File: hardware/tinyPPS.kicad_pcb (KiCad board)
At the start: 2 copper layers, 63 x 37 mm, 63 parts, among them IC1 AP2205-33Y-13, IC2 AP33772SDKZ-13-FA01, J1 USB_C_Receptacle_USB2.0_14P, J2 187-3802, J3 187-3802, J5 SM03B-SRSS-TB_LF__SN_, Q1 DMN3009SFG-7, Q2 DMN3009SFG-7, Q3 BSS123, Q4 BSS123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

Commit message: Minor changes on the PCB
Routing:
- net Net-(Q1-G): track 14.6 -> 13.6 mm
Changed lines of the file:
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@@
 	)
 	(gr_text "DBG"
-		(at 104.35 109.05 0)
+		(at 101.3 108.8 0)
 		(layer "F.SilkS")
 		(effects
@@
 	)
 	(segment
-		(start 118.72 89.32)
-		(end 118.7 89.3)
-		(width 0.3)
-		(layer "F.Cu")
-		(net 80)
-	)
-	(segment
-		(start 118.72 90)
-		(end 118.72 89.32)
+		(start 124.8405 85.7095)
+		(end 124.85 85.7)
 		(width 0.3)
 		(layer "F.Cu")
@@
 	)
 	(segment
-		(start 124.8405 85.7095)
-		(end 124.85 85.7)
+		(start 119.4 90)
+		(end 118.72 90)
 		(width 0.3)
 		(layer "F.Cu")
@@
 	)
 	(via
-		(at 118.7 89.3)
+		(at 119.4 90)
 		(size 0.6)
 		(drill 0.3)
@@
 	)
 	(segment
-		(start 124.85 85.7)
-		(end 124.85 89.3)
+		(start 119.4 90)
+		(end 120.4 91)
 		(width 0.3)
 		(layer "B.Cu")
@@
 	)
 	(segment
-		(start 124.85 89.3)
-		(end 124.85 91)
+		(start 124.85 85.7)
+		(end 124.85 89.3)
 		(width 0.3)
 		(layer "B.Cu")
@@
 	)
 	(segment
-		(start 124.85 91)
-		(end 120.4 91)
+		(start 120.4 91)
+		(end 124.85 91)
 		(width 0.3)
 		(layer "B.Cu")
@@
 	)
 	(segment
-		(start 120.4 91)
-		(end 118.7 89.3)
+		(start 124.85 89.3)
+		(end 124.85 91)
 		(width 0.3)
 		(layer "B.Cu")

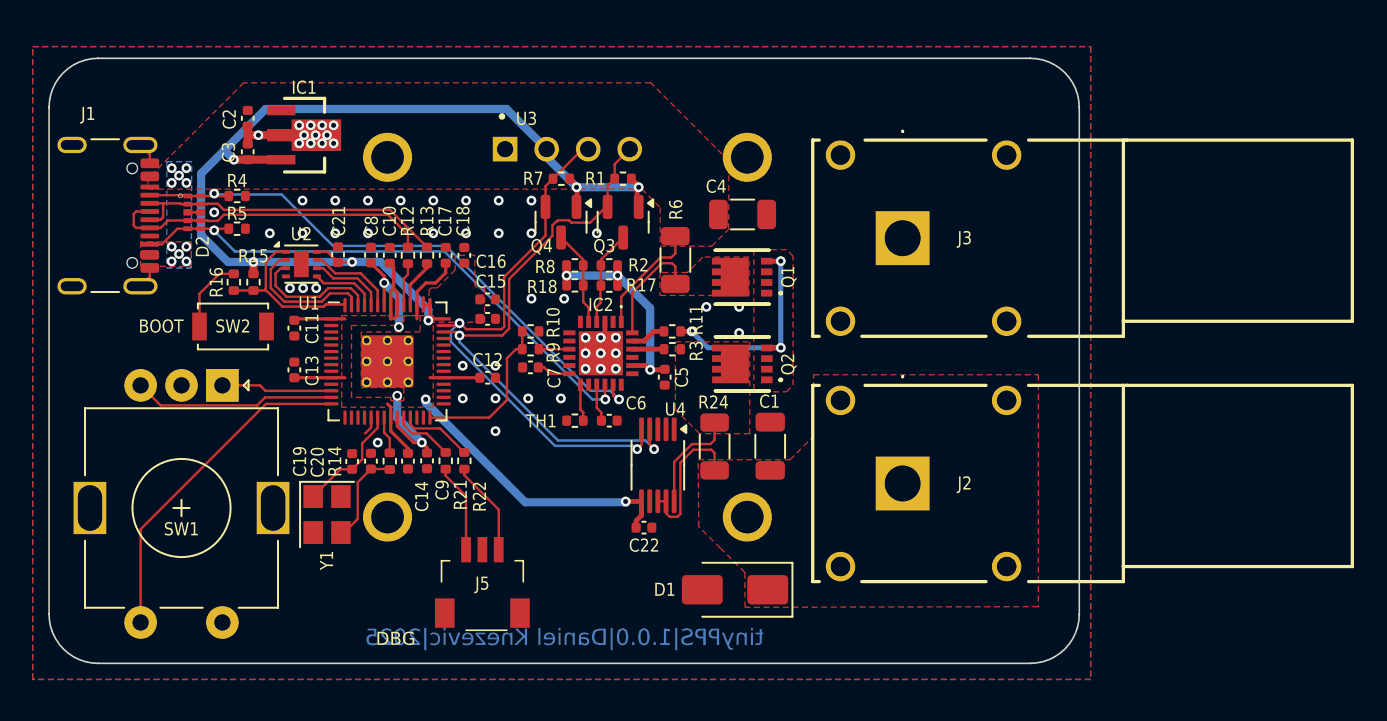
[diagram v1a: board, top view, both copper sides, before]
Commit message: Change rotary encoder to a horizontal type
- Re-route the PCB
- Make PCB with smaller (60mm)
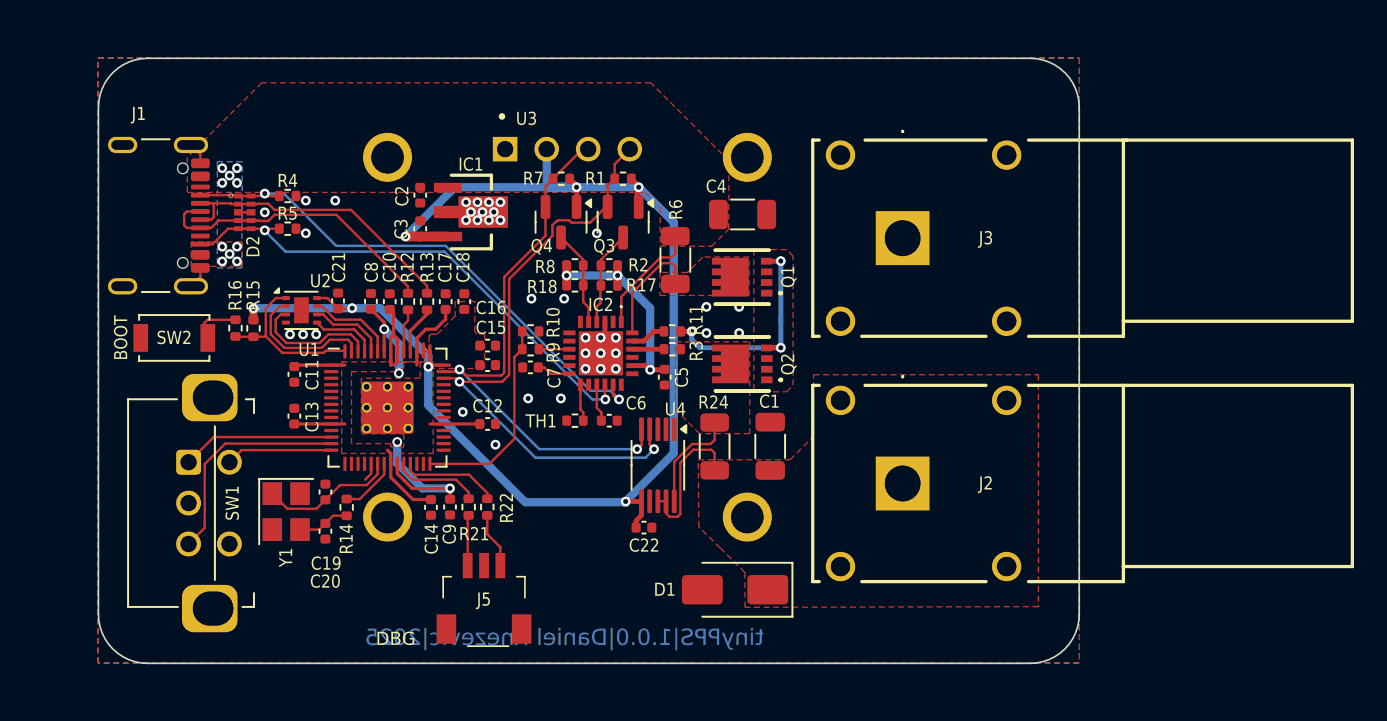
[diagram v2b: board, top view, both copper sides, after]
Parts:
- R3: value 27R -> 100R
- SW1: footprint Rotary_Encoder:RotaryEncoder_Alps_EC11E-Switch_Vertical_H20mm -> Rotary_Encoder:EC11 horizontal
- moved C2 11.5 mm to (102.8, 81.7)
- moved C3 11.5 mm to (102.8, 83.7)
- moved IC1 11.2 mm to (105.9, 82.7)
- moved SW1 6.22 mm to (86.6, 98.0), turned to 0 degrees
- moved C20 5.11 mm to (97.0, 102.2), turned to -90 degrees
- moved R14 3.87 mm to (98.3, 100.8)
- moved SW2 3.66 mm to (87.8, 90.4), turned to 0 degrees
- moved C14 3.16 mm to (103.5, 100.8)
- moved C9 3.16 mm to (104.6, 100.7)
- moved R21 3.16 mm to (105.8, 100.7)
- moved R22 3.16 mm to (106.9, 100.7)
- moved D2 3.09 mm to (92.1, 82.7)
- moved R4 3.09 mm to (94.7, 81.7)
- moved R5 3.09 mm to (94.7, 83.7)
- moved J1 3.09 mm to (85.7, 82.9)
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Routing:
- net /GPIO11: track 20.5 -> 6.53 mm
- net +3V3: track 101.1 -> 105.7 mm, vias 8 -> 7
- net +1V1: track 17.3 -> 20.5 mm
- net /CC2: track 35.2 -> 32.1 mm
- net /CC1: track 35.9 -> 32.8 mm
- net GND: track 9.71 -> 6.79 mm, vias 55 -> 38
- net /PD_INT: track 9.76 -> 12.4 mm
- net /GPIO9: track 6.80 -> 9.36 mm
- net Net-(C20-Pad1): track 5.73 -> 3.20 mm
- net Net-(J5-Pad3): track 5.80 -> 3.40 mm
- net Net-(J5-Pad1): track 5.44 -> 3.10 mm
- net /USB_D+: track 20.0 -> 17.9 mm
- net /SDA: track 36.0 -> 37.8 mm
- net /~{USB_BOOT}: track 4.61 -> 2.89 mm
- net /USB_D-: track 20.0 -> 18.4 mm
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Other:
- board size 63 x 37 mm -> 60 x 37 mm

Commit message: Update PCB routing - use +3v3 and GND planes
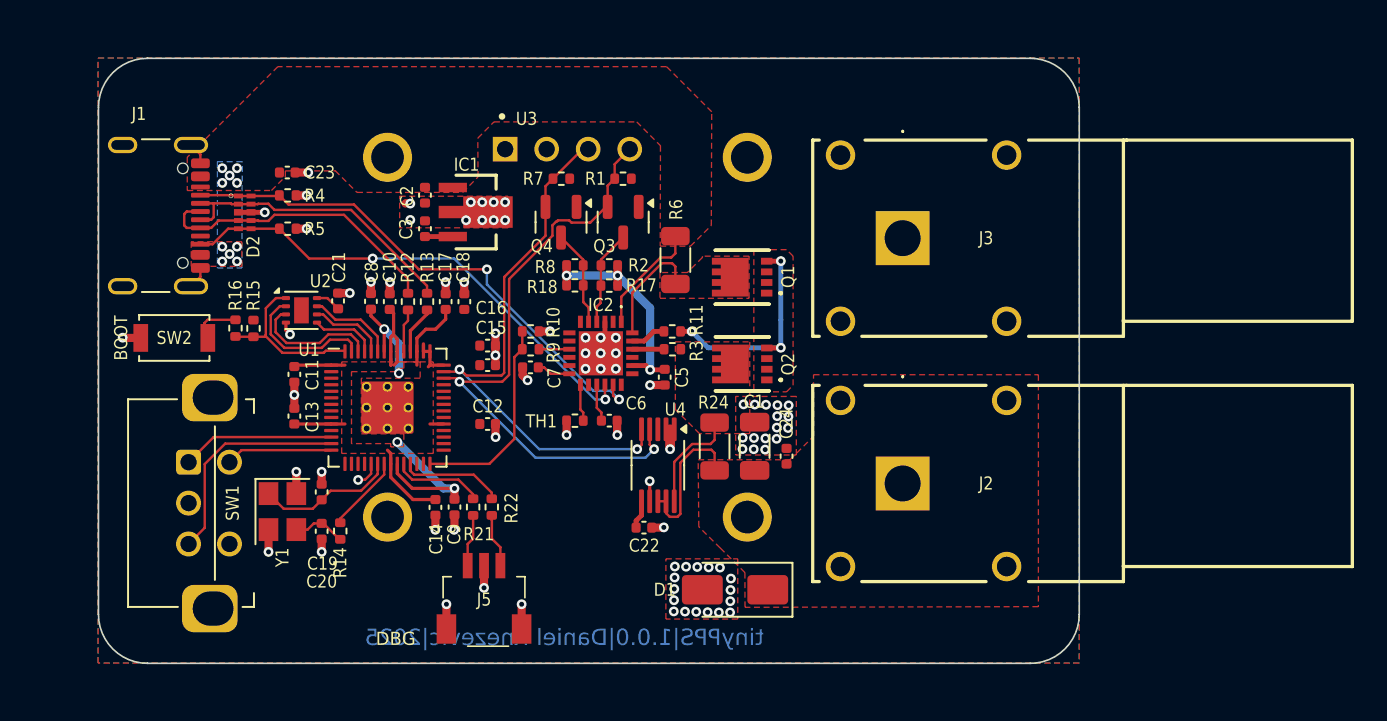
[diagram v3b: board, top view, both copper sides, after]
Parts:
- removed C4: 10u, Capacitor_SMD:C_1206_3216Metric
- added C23: 100n, Capacitor_SMD:C_0402_1005Metric, F.Cu at (94.7, 80.3)
- added C24: 100n, Capacitor_SMD:C_0402_1005Metric, F.Cu at (125.2, 97.6)
- moved R14 1.50 mm to (97.9, 102.2)
- moved C1 0.95 mm to (123.2, 97.0)
- moved C2 0.29 mm to (103.1, 81.7)
- moved C3 0.29 mm to (103.1, 83.7)
- moved IC1 0.29 mm to (106.2, 82.7)
- moved C14 0.27 mm to (103.7, 100.8)
- moved C9 0.27 mm to (104.9, 100.7)
- moved R21 0.27 mm to (106.0, 100.7)
- moved R22 0.27 mm to (107.2, 100.7)
- moved C19 0.23 mm to (96.8, 99.8)
- moved C20 0.23 mm to (96.8, 102.2)
- moved Y1 0.23 mm to (94.4, 101.0)
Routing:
- net +3V3: track 105.7 -> 25.8 mm, vias 7 -> 0
- net GND: track 6.79 -> 38.5 mm, vias 38 -> 85
- net /CC2: track 32.1 -> 30.8 mm
- net Net-(U1-XOUT): track 3.57 -> 4.71 mm
- net +1V1: track 20.5 -> 19.7 mm

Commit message: Change PCB size to 60x40mm and update INA226 circuit
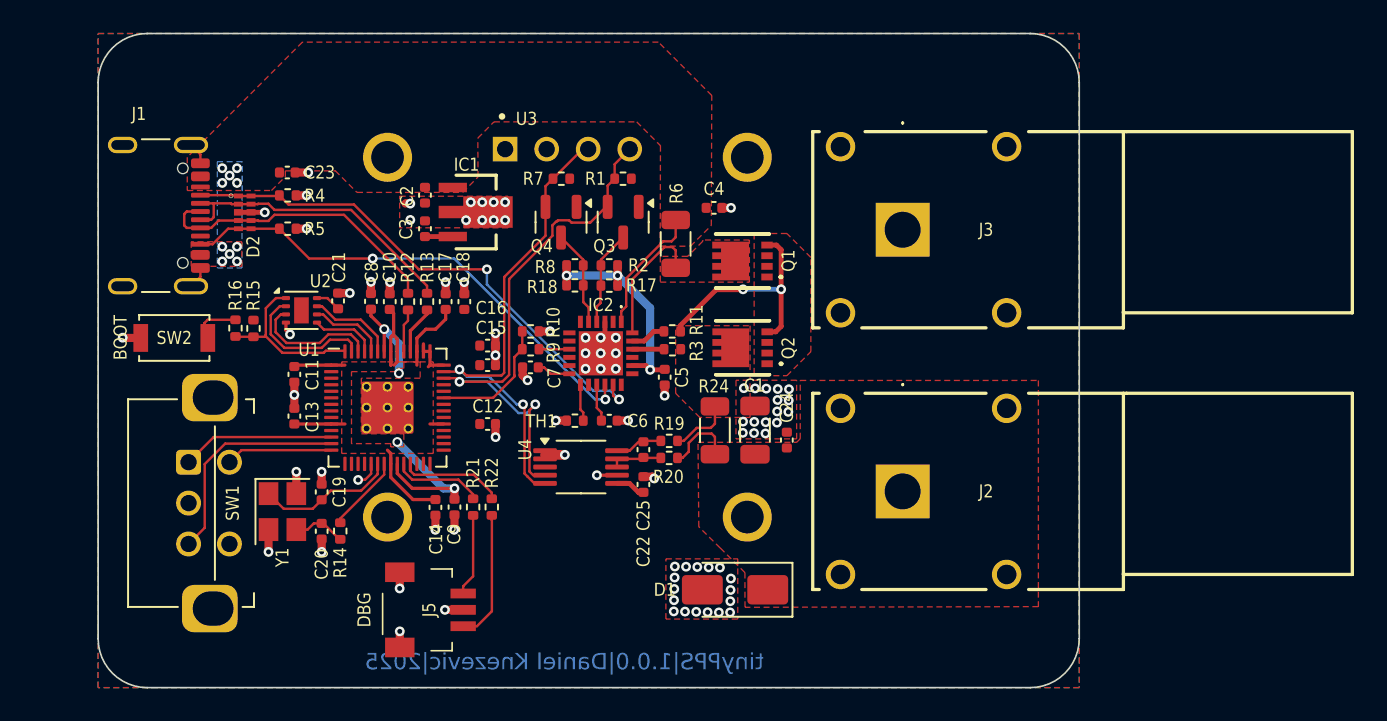
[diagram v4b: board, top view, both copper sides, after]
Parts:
- added C25: 100n, Capacitor_SMD:C_0402_1005Metric, F.Cu at (116.4, 97.2)
- added C4: 1u, Capacitor_SMD:C_0402_1005Metric, F.Cu at (120.8, 82.4)
- added R19: 10R, Resistor_SMD:R_0402_1005Metric, F.Cu at (118.0, 96.7)
- added R20: 10R, Resistor_SMD:R_0402_1005Metric, F.Cu at (118.0, 97.7)
- moved U4 4.70 mm to (112.6, 98.3), turned to 0 degrees
- moved J5 3.75 mm to (103.0, 107.0), turned to -90 degrees
- moved C22 2.64 mm to (116.4, 99.4), turned to 90 degrees
- moved C1 0.99 mm to (123.3, 96.0)
- moved Q1 0.99 mm to (121.2, 85.7)
- moved C24 0.99 mm to (125.2, 96.6)
- moved Q2 0.99 mm to (121.2, 91.0)
- moved R6 0.99 mm to (118.4, 84.6)
- moved R24 0.99 mm to (120.8, 96.0)
- moved J3 0.52 mm to (132.3, 83.8)
- moved J2 0.48 mm to (132.3, 99.8)
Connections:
- C1 pad 1: /VBUS_PD -> /VOUT_PD
- C24 pad 1: /VBUS_PD -> /VOUT_PD
- D1 pad 1: /VBUS_PD -> /VOUT_PD
- J2 pad 1: /VBUS_PD -> /VOUT_PD
- J2 pad 2: /VBUS_PD -> /VOUT_PD
- J2 pad 3: /VBUS_PD -> /VOUT_PD
- J2 pad 4: /VBUS_PD -> /VOUT_PD
- J2 pad 5: /VBUS_PD -> /VOUT_PD
- R24 pad 2: /VBUS_PD -> /VOUT_PD
- U1 pad 28: /PD_INT -> unconnected-(U1-GPIO17-Pad28)
- U1 pad 37: unconnected-(U1-GPIO25-Pad37) -> /PD_INT
- U4 pad 10: /VIN+ -> Net-(U4-Vin+)
- U4 pad 8: /VBUS_PD -> Net-(U4-Vbus)
- U4 pad 9: /VBUS_PD -> Net-(U4-Vbus)
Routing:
- net /VBUS_PD: track 8.42 -> 0.00 mm
- net /PD_INT: track 12.4 -> 7.63 mm
- net Net-(J5-Pad3): track 3.29 -> 8.00 mm
- net /SDA: track 37.8 -> 33.6 mm
- net /VOUT_PD: track 0.00 -> 3.81 mm
- net /SCL: track 34.2 -> 30.6 mm
- net Net-(U4-Vbus): track 0.00 -> 3.24 mm
- net /VIN+: track 6.06 -> 3.34 mm
- net Net-(U4-Vin+): track 0.00 -> 2.68 mm
- net Net-(J5-Pad1): track 3.21 -> 5.03 mm
- net GND: track 38.5 -> 37.1 mm, vias 85 -> 86
- net Net-(IC2-VCC): track 6.43 -> 7.34 mm
- net VBUS: track 6.45 -> 7.36 mm
- net Net-(Q1-G): track 13.6 -> 14.1 mm, vias 3 -> 2
- added copper zone on F.Cu, net /VOUT_PD
- removed copper zone on F.Cu, net /VBUS_PD
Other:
- board size 60 x 37 mm -> 60 x 40 mm

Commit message: Change footprint for flash to WSON-8 6x5mm and re-route the PCB
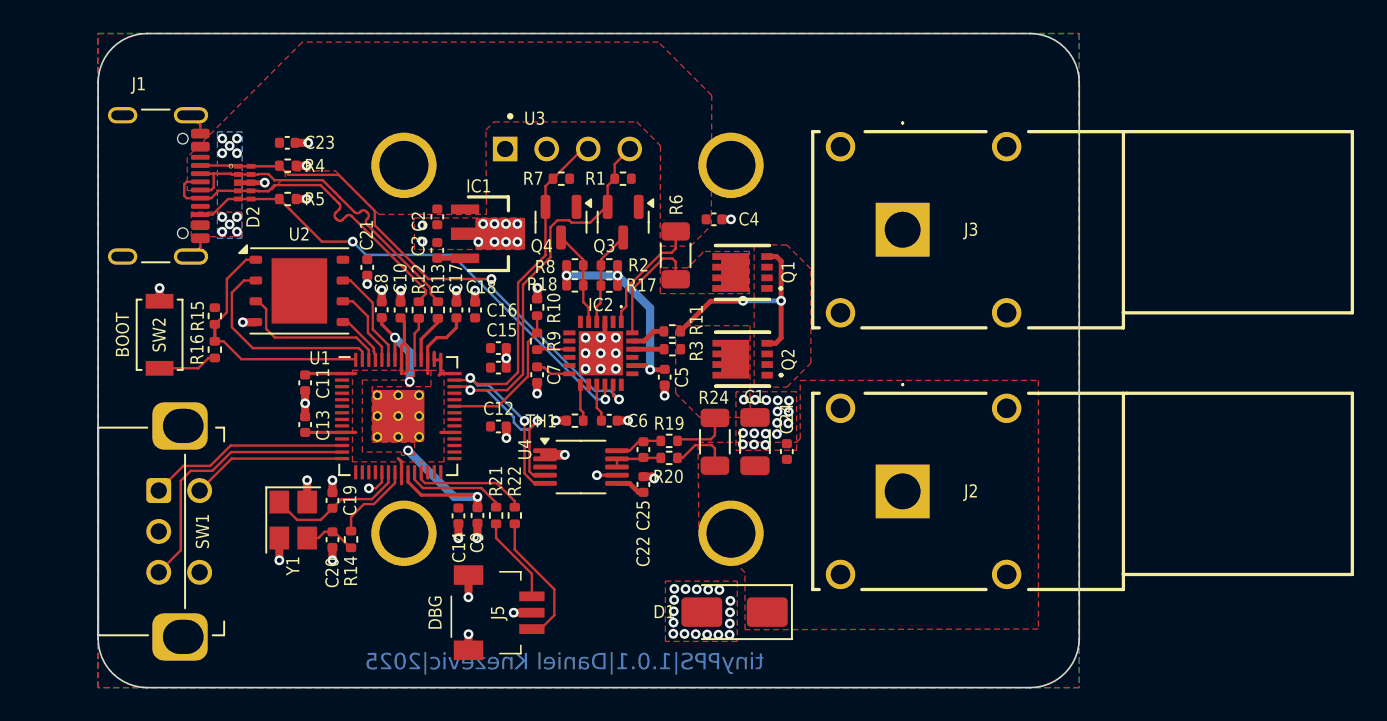
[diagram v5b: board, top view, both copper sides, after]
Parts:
- U2: footprint Package_SON:WSON-8-1EP_2x2mm_P0.5mm_EP0.9x1.6mm -> Package_SON:WSON-8-1EP_6x5mm_P1.27mm_EP3.4x4mm
- moved U3 18.0 mm to (99.3, 77.3)
- moved J5 4.21 mm to (107.2, 107.2)
- moved C21 2.72 mm to (99.6, 86.1), turned to -90 degrees
- moved SW1 2.52 mm to (84.8, 99.7)
- moved R15 2.48 mm to (90.2, 89.1)
- moved R16 1.82 mm to (90.2, 91.1), turned to -90 degrees
- moved C23 1.82 mm to (94.7, 78.5)
- moved D2 1.82 mm to (92.1, 80.9)
- moved J1 1.82 mm to (85.7, 81.1)
- moved R4 1.82 mm to (94.7, 79.9)
- moved R5 1.82 mm to (94.7, 81.9)
- moved C3 1.52 mm to (103.8, 85.0)
- moved C2 1.52 mm to (103.8, 83.0)
- moved IC1 1.52 mm to (106.9, 84.0)
- moved R10 1.52 mm to (109.9, 88.5), turned to 90 degrees
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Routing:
- net /QSPI_SS: track 10.2 -> 15.4 mm
- net +3V3: track 25.9 -> 21.0 mm
- net /QSPI_SD1: track 8.40 -> 13.0 mm
- net /USB_D+: track 18.1 -> 21.4 mm
- net /GPIO10: track 13.6 -> 16.7 mm
- net /GPIO11: track 6.53 -> 9.52 mm
- net /GPIO9: track 9.36 -> 12.4 mm
- net /USB_D-: track 18.4 -> 20.6 mm
- net +1V1: track 19.7 -> 21.8 mm
- net GND: track 37.1 -> 35.3 mm, vias 86 -> 85
- net /PD_INT: track 7.63 -> 9.32 mm
- net /SCL: track 30.6 -> 29.1 mm
- net /QSPI_SD2: track 7.84 -> 9.19 mm
- net /SDA: track 33.6 -> 32.4 mm
- net /CC1: track 32.4 -> 33.4 mm
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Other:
- board text added: "tinyPPS|1.0.1|Daniel Knezevic|2025"
- board text removed: "tinyPPS|1.0.0|Daniel Knezevic|2025"

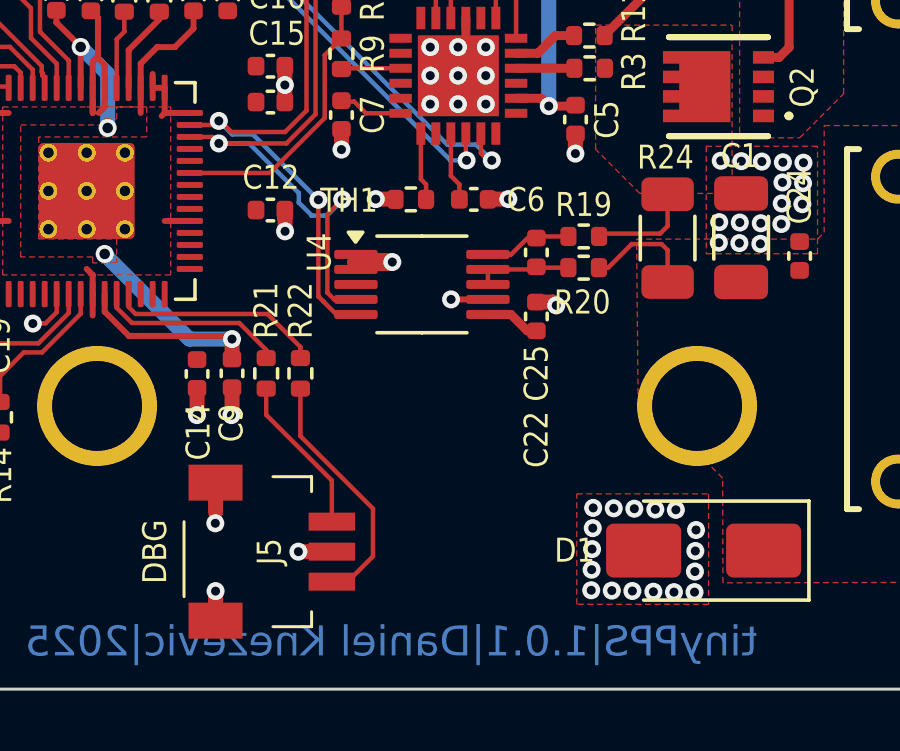
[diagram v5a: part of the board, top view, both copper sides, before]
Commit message: Fix reading current from INA226
- Remove output filterfing from INA266, cause it may not be correctly
  implemented.
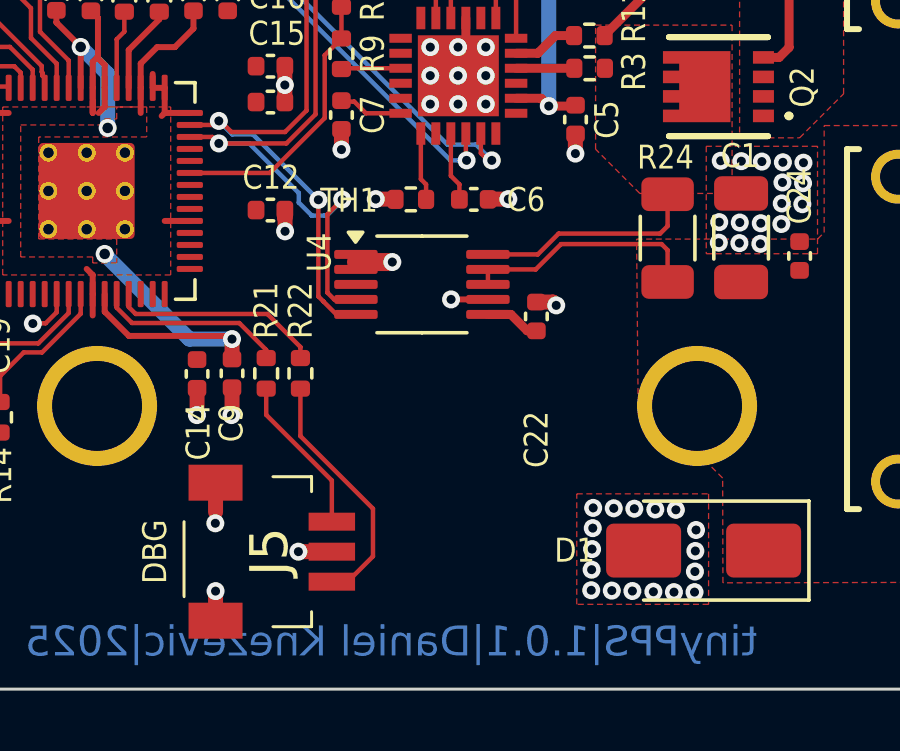
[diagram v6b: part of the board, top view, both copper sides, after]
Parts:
- removed C25: 100n, Capacitor_SMD:C_0402_1005Metric
- removed R19, R20: 10R, Resistor_SMD:R_0402_1005Metric
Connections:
- U4 pad 10: Net-(U4-Vin+) -> /VIN+
- U4 pad 8: Net-(U4-Vbus) -> /VOUT_PD
- U4 pad 9: Net-(U4-Vbus) -> /VOUT_PD
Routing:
- net /VOUT_PD: track 3.21 -> 7.45 mm
- net /VIN+: track 3.05 -> 7.00 mm
- net Net-(U4-Vbus): track 3.24 -> 0.00 mm
- net Net-(U4-Vin+): track 2.68 -> 0.00 mm
